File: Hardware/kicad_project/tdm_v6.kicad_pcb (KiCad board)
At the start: 4 copper layers, 65 x 100 mm, 218 parts, among them J1 picoprobe_debug, J2 USB_C_Receptacle_USB2.0, J3 line_in, J4 headphone_out, J5 midi_in, J6 midi_out, J7 battery, J8 Conn_01x02_Female, Q1 DMG2305UX-13, Q2 Q_PMOS_GSD, Q3 Q_NMOS_GSD, Q4 Q_NMOS_GSD, SW1 spst_4_pin_internal, SW10 spst_4_pin_internal, SW11 spst_4_pin_internal, SW12 spst_4_pin_internal, SW13 spst_4_pin_internal, SW14 spst_4_pin_internal, SW15 spst_4_pin_internal, SW16 spst_4_pin_internal, SW17 spst_4_pin_internal, SW18 spst_4_pin_internal, SW19 spst_4_pin_internal, SW2 spst_4_pin_internal, SW20 spst_4_pin_internal, SW21 spst_4_pin_internal, SW22 spst_4_pin_internal, SW23 spst_4_pin_internal, SW24 spst_4_pin_internal, SW25 spst_4_pin_internal, SW26 spst_4_pin_internal, SW27 spst_4_pin_internal, SW3 spst_4_pin_internal, SW4 spst_4_pin_internal, SW5 spst_4_pin_internal, SW6 spst_4_pin_internal, SW7 spst_4_pin_internal, SW8 spst_4_pin_internal, SW9 spst_4_pin_internal, U1 W25Q32JVSS, U11 ME6211C, U2 RP2040, U3 TLV320AIC3204, U4 AP3722AT_mic, U5 HCPL-0631, U6 MCP73831T-2ATI_OT, U7 LM4040DBZ-2.5, U9 ME6211C, Y1 Crystal_GND24

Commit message: v11 hardware
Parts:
- R4, R5: value 4.7k -> 3.3k
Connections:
- C54 pad 1: Net-(C54-Pad1) -> 3v3_filter
- C60 pad 1: VBUS -> VSYS
- C64 pad 1: VBUS -> VSYS
- LCD1 pad 8: Net-(C54-Pad1) -> 3v3_filter
- Q2 pad 3: VBUS -> VSYS
- U11 pad 1: VBUS -> VSYS
- U11 pad 3: VBUS -> VSYS
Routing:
- net VSYS: track 0.00 -> 15.4 mm, vias 0 -> 2
- net VBUS: track 79.0 -> 63.7 mm, vias 7 -> 4
- net 3v3_filter: track 421.1 -> 434.2 mm, vias 25 -> 27
- net Net-(C54-Pad1): track 9.80 -> 0.00 mm, vias 2 -> 0
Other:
- board text added: "V11"
- board text removed: "V10"

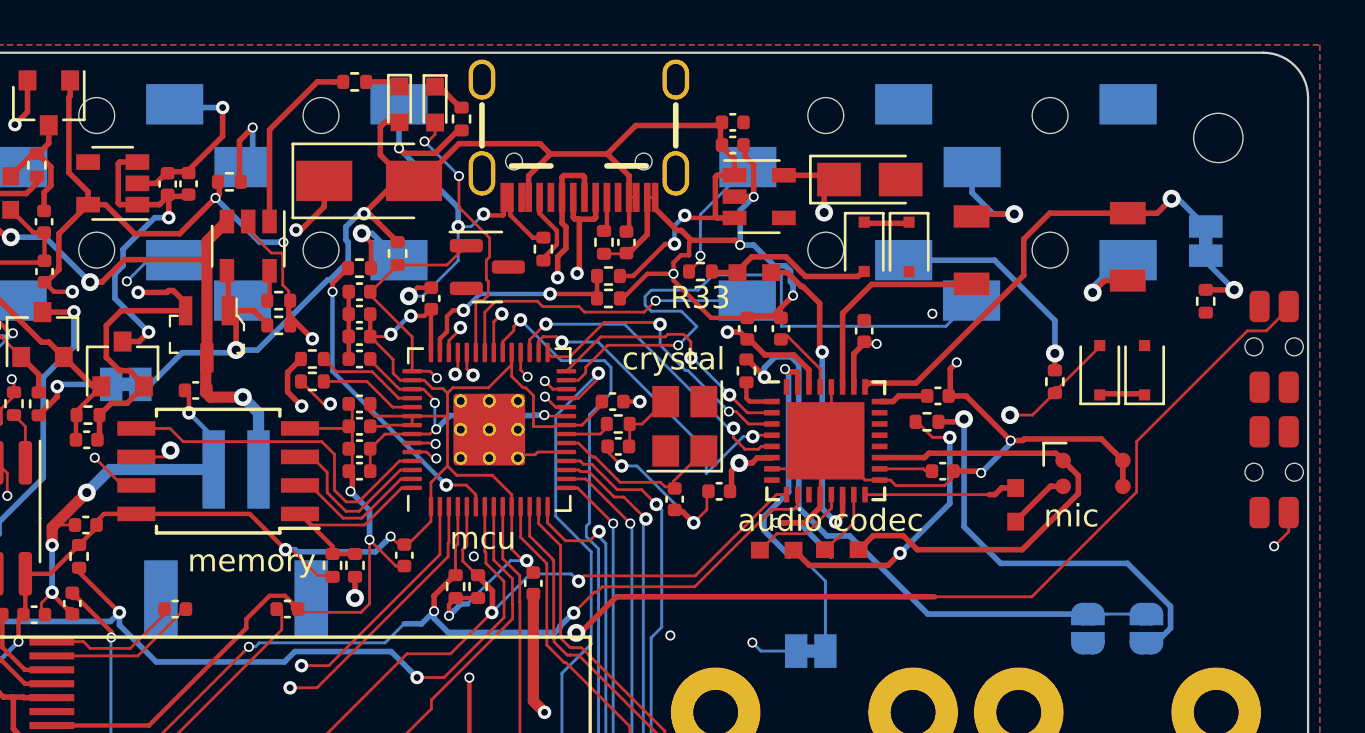
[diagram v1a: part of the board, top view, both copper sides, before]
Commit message: pcb bodge fixes
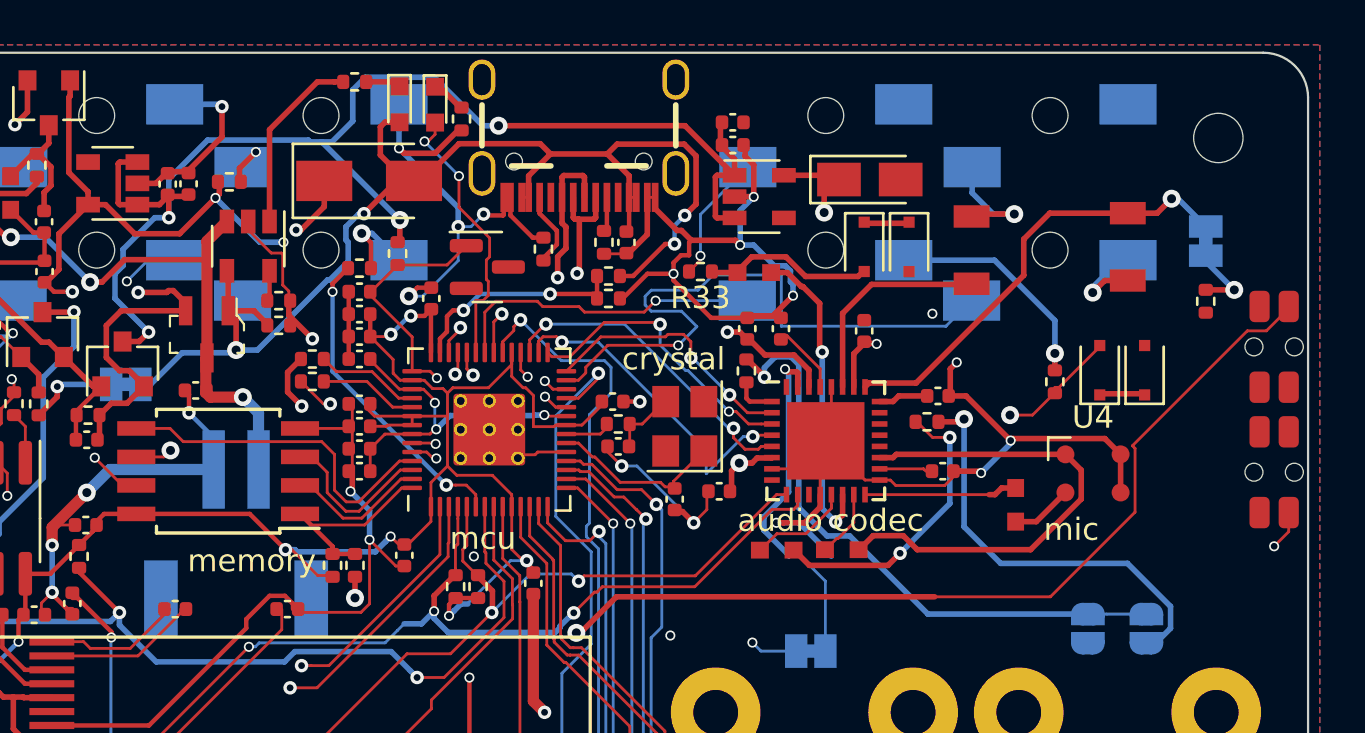
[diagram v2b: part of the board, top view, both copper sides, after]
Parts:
- D2: value LED -> LEDGreen
- R23: value 5k -> 5.1k
- U4: footprint RandomJunk:AP3722AT-SMD-mic -> MyLibrary:LGA-4(3x3.8)
- turned U4 to 0 degrees
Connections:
- C5 pad 1: VBUS -> VSYS
- C63 pad 1: VBUS -> VSYS
- R22 pad 2: VBUS -> VSYS
- U9 pad 1: VBUS -> VSYS
- U9 pad 3: VBUS -> VSYS
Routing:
- net VSYS: track 15.4 -> 58.9 mm, vias 2 -> 4
- net VBUS: track 63.7 -> 55.1 mm
- net Net-(J6-Pad3): track 4.61 -> 2.54 mm
- net Net-(R6-Pad2): track 50.7 -> 51.2 mm
- net Net-(C45-Pad2): track 21.5 -> 22.0 mm
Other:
- board text added: "V12"
- board text removed: "V11"
